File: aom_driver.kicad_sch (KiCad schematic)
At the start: 34 parts, among them J1 Conn_Coaxial, J2 Conn_Coaxial, J3 Screw_Terminal_01x03, J4 Screw_Terminal_01x03, U1 LT3082xDD, U2 ADP7182AUJZ-5.0, U3 M3SWA-2-50

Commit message: v2
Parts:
- added C1, C11, C12, C13, C14, C15, C16, C17, C18, C2, C20, C22, C23, C24, C27, C28, C29, C3, C30, C31, C32, C33, C34, C35, C36, C39, C4, C40, C41, C42, C43, C44, C45, C46, C5, C55, C6: 2.2u, Capacitor_SMD:C_0805_2012Metric_Pad1.18x1.45mm_HandSolder, symbol Device:C
- added C10, C19, C21, C25, C26, C37, C38, C51, C52, C7, C8, C9: 0.1u, Capacitor_SMD:C_0805_2012Metric_Pad1.18x1.45mm_HandSolder, symbol Device:C
- added D1, D2, D3, D4, D5, D6: LED, LED_SMD:LED_0603_1608Metric_Pad1.05x0.95mm_HandSolder, symbol Device:LED
- added FL1: RLP-320+, RF_Mini-Circuits:Mini-Circuits_GP731_LandPatternPL-176, symbol RF_Filter:RLP-158
- added FL2: RLP-158, RF_Mini-Circuits:Mini-Circuits_GP731_LandPatternPL-176, symbol RF_Filter:RLP-158
- added L1, L2: 10u, Inductor_SMD:L_0805_2012Metric_Pad1.05x1.20mm_HandSolder, symbol Device:L
- added R1, R17, R18, R19, R2, R20, R29, R3, R30, R33, R34, R4, R42, R44, R54, R55, R8: 0, Resistor_SMD:R_0805_2012Metric_Pad1.20x1.40mm_HandSolder, symbol Device:R
- added R10, R21, R22, R35, R36, R37, R38, R9: 499k, Resistor_SMD:R_0805_2012Metric_Pad1.20x1.40mm_HandSolder, symbol Device:R
- added R11, R12, R25, R26, R39, R40: 4.7k, Resistor_SMD:R_0805_2012Metric_Pad1.20x1.40mm_HandSolder, symbol Device:R
- added R13, R14, R15, R16, R27, R28, R31, R32, R45: 1.5k, Resistor_SMD:R_0805_2012Metric_Pad1.20x1.40mm_HandSolder, symbol Device:R
- added R23, R24: 2.7M, Resistor_SMD:R_0805_2012Metric_Pad1.20x1.40mm_HandSolder, symbol Device:R
- added R41, R43: 49.9, Resistor_SMD:R_0805_2012Metric_Pad1.20x1.40mm_HandSolder, symbol Device:R
- added R5: 10M, Resistor_SMD:R_0805_2012Metric_Pad1.20x1.40mm_HandSolder, symbol Device:R
- added R6: 49.9k, Resistor_SMD:R_0805_2012Metric_Pad1.20x1.40mm_HandSolder, symbol Device:R
- added R7: 150k, Resistor_SMD:R_0805_2012Metric_Pad1.20x1.40mm_HandSolder, symbol Device:R
- added RV1, RV2: 2M, Potentiometer_THT:Potentiometer_Bourns_3296X_Horizontal, symbol Device:R_Potentiometer
- added SYM1: Logo_Open_Hardware_Small, Symbol:OSHW-Logo2_9.8x8mm_SilkScreen, symbol Graphic:Logo_Open_Hardware_Small
- added SYM2: Logo_Open_Hardware_Small, Symbol:KiCad-Logo2_5mm_SilkScreen, symbol Graphic:Logo_Open_Hardware_Small
- added TP1, TP10, TP11, TP12, TP13, TP14, TP15, TP16, TP17, TP18, TP19, TP2, TP20, TP21, TP22, TP3, TP4, TP5, TP6, TP7, TP8, TP9: TestPoint, TestPoint:TestPoint_Pad_D2.0mm, symbol Connector:TestPoint
- added U1, U10, U2, U3, U4, U5, U6, U9: LT3082xDD, Package_DFN_QFN:DFN-8-1EP_3x3mm_P0.5mm_EP1.66x2.38mm, symbol Regulator_Linear:LT3082xDD
- added U11, U12: GVA-81, Package_TO_SOT_SMD:SOT-89-3, symbol RF_Amplifier:GVA-81
- added U13, U14: RVA-3000R, RF_Mini-Circuits:Mini-Circuits_DV874_LandPatternPL-040, symbol RF:RVA-3000R
- added U15, U16: ADP7182AUJZ-5.0, Package_TO_SOT_SMD:TSOT-23-5, symbol Regulator_Linear:ADP7182AUJZ-5.0
- added U17, U18: M3SWA-2-50, Package_DFN_QFN:Mini-Circuits_DL805, symbol RF_Switch:M3SWA-2-50
- added U7, U8: PAT1220-C-8DB, RF_Converter:RF_Attenuator_Susumu_PAT1220, symbol RF:PAT1220-C-8DB
- added X1, X2: CVCO55xx, RF_Mini-Circuits:Mini-Circuits_CK605_LandPatternPL-012, symbol Oscillator:CVCO55xx
- R46: renamed from R5; value 432 -> 4.7k; DKPN 311-432CRCT-ND -> 13-RC0805FR-134K7LCT-ND; MFPN RC0805FR-07432RL -> RC0805FR-134K7L
- R47: renamed from R4; value 432 -> 4.7k; DKPN 311-432CRCT-ND -> 13-RC0805FR-134K7LCT-ND; MFPN RC0805FR-07432RL -> RC0805FR-134K7L
- R48: renamed from R7; value 2.43k -> 27k; DKPN 311-2.43KCRCT-ND -> 311-27.0KCRCT-ND; MFPN RC0805FR-072K43L -> RC0805FR-0727KL
- R49: renamed from R8; value 2.43k -> 27k; DKPN 311-2.43KCRCT-ND -> 311-27.0KCRCT-ND; MFPN RC0805FR-072K43L -> RC0805FR-0727KL
- U20: renamed from U2; DKPN 505-ADP7182ACPZ-5.0-R7CT-ND -> 505-ADP7182AUJZ-5.0-R7CT-ND; MFPN ADP7182ACPZ-5.0-R7 -> ADP7182AUJZ-5.0-R7
- renumbered C3 to C47, C4 to C48, C6 to C49, C5 to C50, C2 to C53, C1 to C54, D4 to D10, D2 to D7, D1 to D8, D3 to D9, R6 to R50, R2 to R51, R3 to R52, R1 to R53, TP3 to TP23, TP4 to TP24, TP2 to TP25, TP1 to TP26, U3 to U19, U1 to U21
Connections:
- net +5V_SW: now also R45.1
- net GND: now also C1.2, C10.2, C11.2, C12.2, C13.2, C14.2, C15.2, C16.2, C17.2, C18.2, C19.2, C2.2, C21.2, C23.2, C24.2, C25.2, C26.2, C29.2, C3.2, C30.2, C31.2, C32.2, C35.1, C36.1, C37.1, C38.1, C4.2, C41.1, C42.1, C45.2, C46.2, C5.2, C51.2, C52.1, C6.2, C7.2, C8.2, C9.2, D1.1 (K), D2.1 (K), D3.1 (K), D4.1 (K), D5.2 (A), D6.2 (A), FL1.1 (GND), FL1.3 (GND), FL1.4 (GND), FL1.5 (GND), FL1.7 (GND), FL1.8 (GND), FL2.1 (GND), FL2.3 (GND), FL2.4 (GND), FL2.5 (GND), FL2.7 (GND), FL2.8 (GND), R10.2, R13.2, R14.2, R15.2, R16.2, R21.2, R22.2, R23.2, R24.2, R27.2, R28.2, R31.2, R32.2, R35.1, R36.1, R41.2, R43.2, R45.2, R6.1, R8.2, R9.2, RV1.2, RV1.3, RV2.2, RV2.3, U11.2 (GND), U12.2 (GND), U13.1 (GND), U13.11 (GND), U13.12 (GND), U13.13 (GND), U13.15 (GND), U13.16 (GND), U13.3 (GND), U13.4 (GND), U13.5 (GND), U13.7 (GND), U13.8 (GND), U13.9 (GND), U14.1 (GND), U14.11 (GND), U14.12 (GND), U14.13 (GND), U14.15 (GND), U14.16 (GND), U14.3 (GND), U14.4 (GND), U14.5 (GND), U14.7 (GND), U14.8 (GND), U14.9 (GND), U15.1 (GND), U16.1 (GND), U17.3 (TTL_GND), U17.8 (GND), U17.9 (GND), U18.3 (TTL_GND), U18.8 (GND), U18.9 (GND), U7.3, U8.3, X1.1 (GND), X1.11 (GND), X1.12 (GND), X1.13 (GND), X1.15 (GND), X1.16 (GND), X1.3 (GND), X1.4 (GND), X1.5 (GND), X1.6 (GND), X1.7 (GND), X1.8 (GND), X1.9 (GND), X2.1 (GND), X2.11 (GND), X2.12 (GND), X2.13 (GND), X2.15 (GND), X2.16 (GND), X2.3 (GND), X2.4 (GND), X2.5 (GND), X2.6 (GND), X2.7 (GND), X2.8 (GND), X2.9 (GND)
- net VDD: now also C1.1, C2.1, R1.1, R17.1, R18.1, R19.1, R2.1, R20.1, R3.1, R4.1, R54.1; no longer C53.1, U21.7 (IN), U21.8 (IN)
- net VEE: now also R33.2, R34.2, R55.2; no longer C54.2, U20.2 (VIN)
- net at R51.1, U21.4 (SET): now also C51.1
- net at R52.2, R53.2, U20.3 (EN): now also C52.2
- net at U19.6 (RF-IN): now also C55.1; no longer J1.1 (In)
- net F1/F_OUT: no longer names the net of C48.1
- net F1/F_OUT: now also TP22.1, U18.6 (RF-IN)
- net F2/F_OUT: no longer names the net of C47.1
- net F2/F_OUT: now also TP21.1, U17.6 (RF-IN)
- net SW: no longer names the net of J2.1 (In), R50.1, U19.2 (TTL-IN)
- net SW: now also U17.2 (TTL-IN), U18.2 (TTL-IN)
- new net: C34.1, L2.2, U12.3
- new net: C34.2, TP14.1, U14.2 (RF_IN)
- new net: C35.2, R33.1, U15.2 (VIN)
- new net: C37.2, R35.2, R37.2, U15.3 (EN)
- new net: C40.1, U14.10 (RF_OUT)
- new net: C5.1, R3.2, U1.7 (IN), U1.8 (IN)
- new net: C54.2, R55.1, U20.2 (VIN)
- new net: C25.1, R23.1, RV1.1, U9.4 (SET)
- new net: C17.1, R19.2, U9.7 (IN), U9.8 (IN)
- new net: C45.1, R42.2, U17.5 (VDD)
- new net: C38.2, R36.2, R38.2, U16.3 (EN)
- new net: C33.1, L1.2, U11.3
- new net: C33.2, TP13.1, U13.2 (RF_IN)
- new net: C16.1, R18.2, U6.7 (IN), U6.8 (IN)
- new net: D4.2 (A), R26.2
- new net: C22.2, TP6.1, U8.1
- new net: C28.1, U8.2
- new net: C6.1, R4.2, U3.7 (IN), U3.8 (IN)
- new net: D6.1 (K), R40.1
- new net: C28.2, TP10.1, U12.1
- new net: C27.2, TP9.1, U11.1
- new net: C10.1, R10.1, U3.4 (SET)
- new net: C7.1, R5.1, U2.4 (SET)
- new net: C53.1, R54.2, U21.7 (IN), U21.8 (IN)
- new net: C39.1, U13.10 (RF_OUT)
- new net: D3.2 (A), R25.2
- new net: C22.1, X2.10 (RFout)
- new net: C19.1, R21.1, U5.4 (SET)
- new net: C4.1, R2.2, U4.7 (IN), U4.8 (IN)
- new net: R41.1, U18.1 (RF-OUT1)
- new net: C15.1, R17.2, U5.7 (IN), U5.8 (IN)
- new net: C9.1, R9.1, U1.4 (SET)
- new net: C46.1, R44.2, U18.5 (VDD)
- new net: C3.1, R1.2, U2.7 (IN), U2.8 (IN)
- new net: D5.1 (K), R39.1
- new net: C39.2, FL1.2 (IN), TP15.1
- new net: C36.2, R34.1, U16.2 (VIN)
- new net: D1.2 (A), R11.2
- new net: R7.2, R8.1
- new net: D2.2 (A), R12.2
- new net: C18.1, R20.2, U10.7 (IN), U10.8 (IN)
- new net: C20.2, TP5.1, U7.1
- new net: C27.1, U7.2
- new net: C21.1, R22.1, U6.4 (SET)
- new net: L1.1, R29.2
- new net: C44.2, TP19.1, U18.4 (RF-OUT2)
- new net: C20.1, X1.10 (RFout)
- new net: C8.1, R7.1, U4.4 (SET)
- new net: C26.1, R24.1, RV2.1, U10.4 (SET)
- new net: C44.1, FL2.6 (OUT)
- new net: R5.2, R6.2
- new net: L2.1, R30.2
- new net: C43.2, TP20.1, U17.1 (RF-OUT1)
- new net: C43.1, FL1.6 (OUT)
- new net: R43.1, U17.4 (RF-OUT2)
- new net: C40.2, FL2.2 (IN), TP16.1
- new net: C55.2, J1.1 (In)
- new net +5V_CH1: C23.1, C29.1, R25.1, R27.1, R29.1, R37.1, R42.1, TP7.1, U13.14 (V+), U5.1 (OUT), U5.2 (OUT), U5.9 (OUT)
- new net +5V_CH2: C24.1, C30.1, R26.1, R28.1, R30.1, R38.1, R44.1, TP8.1, U14.14 (V+), U6.1 (OUT), U6.2 (OUT), U6.9 (OUT)
- new net -5V_CH1: C41.2, R39.2, TP17.1, U15.5 (VOUT), U17.7 (VEE)
- new net -5V_CH2: C42.2, R40.2, TP18.1, U16.5 (VOUT), U18.7 (VEE)
- new net VCO_TUNE_CH1: C12.1, R13.1, TP1.1, U2.1 (OUT), U2.2 (OUT), U2.9 (OUT), X1.2 (Vtune)
- new net VCO_TUNE_CH2: C14.1, R14.1, TP2.1, U4.1 (OUT), U4.2 (OUT), U4.9 (OUT), X2.2 (Vtune)
- new net VDD_VCO_CH1: C11.1, R11.1, R15.1, TP3.1, U1.1 (OUT), U1.2 (OUT), U1.9 (OUT), X1.14 (Vcc)
- new net VDD_VCO_CH2: C13.1, R12.1, R16.1, TP4.1, U3.1 (OUT), U3.2 (OUT), U3.9 (OUT), X2.14 (Vcc)
- new net VVA_TUNE_CH1: C31.1, R31.1, TP11.1, U13.6 (V_CTRL), U9.1 (OUT), U9.2 (OUT), U9.9 (OUT)
- new net VVA_TUNE_CH2: C32.1, R32.1, TP12.1, U10.1 (OUT), U10.2 (OUT), U10.9 (OUT), U14.6 (V_CTRL)
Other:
- removed sheet F1
- removed sheet F2
- moved on the sheet: C47, C48, C49, C50, C53, C54, D10, D7, D8, D9, DRA1, H1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

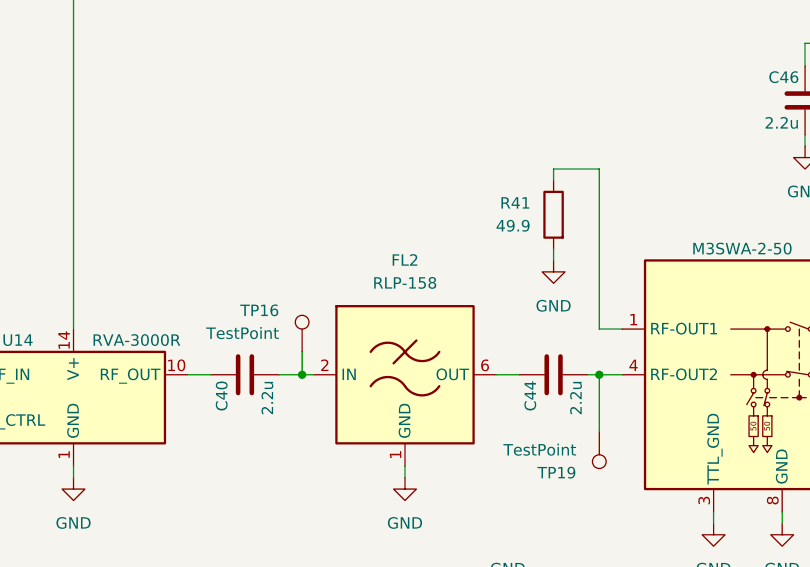
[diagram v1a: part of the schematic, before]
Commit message: Add details to README; add PCB BOM, schematic, PCB image
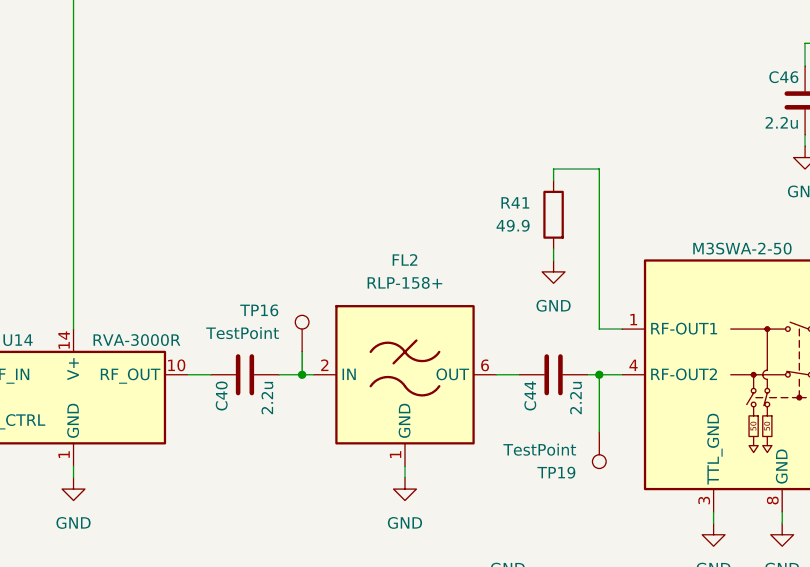
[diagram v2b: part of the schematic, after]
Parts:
- FL2: value RLP-158 -> RLP-158+
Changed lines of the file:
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@@
     (title "AOM driver")
     (date "2023-12-24")
-    (rev "v1")
+    (rev "v2")
     (company "Jacob Feder")
   )
@@
       (effects (font (size 1.27 1.27)))
     )
-    (property "Value" "RLP-158" (at 321.31 284.48 0)
+    (property "Value" "RLP-158+" (at 321.31 284.48 0)
       (effects (font (size 1.27 1.27)))
     )
